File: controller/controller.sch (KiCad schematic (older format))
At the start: 0 parts

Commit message: Add more stuff to controller, start sourcing parts
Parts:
- added U5: ATMEGA328P-AU, TQFP32, symbol ATMEGA328P-AU
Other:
- note added: "TODO: pakeisti kaip reikia Eugenijui\n"

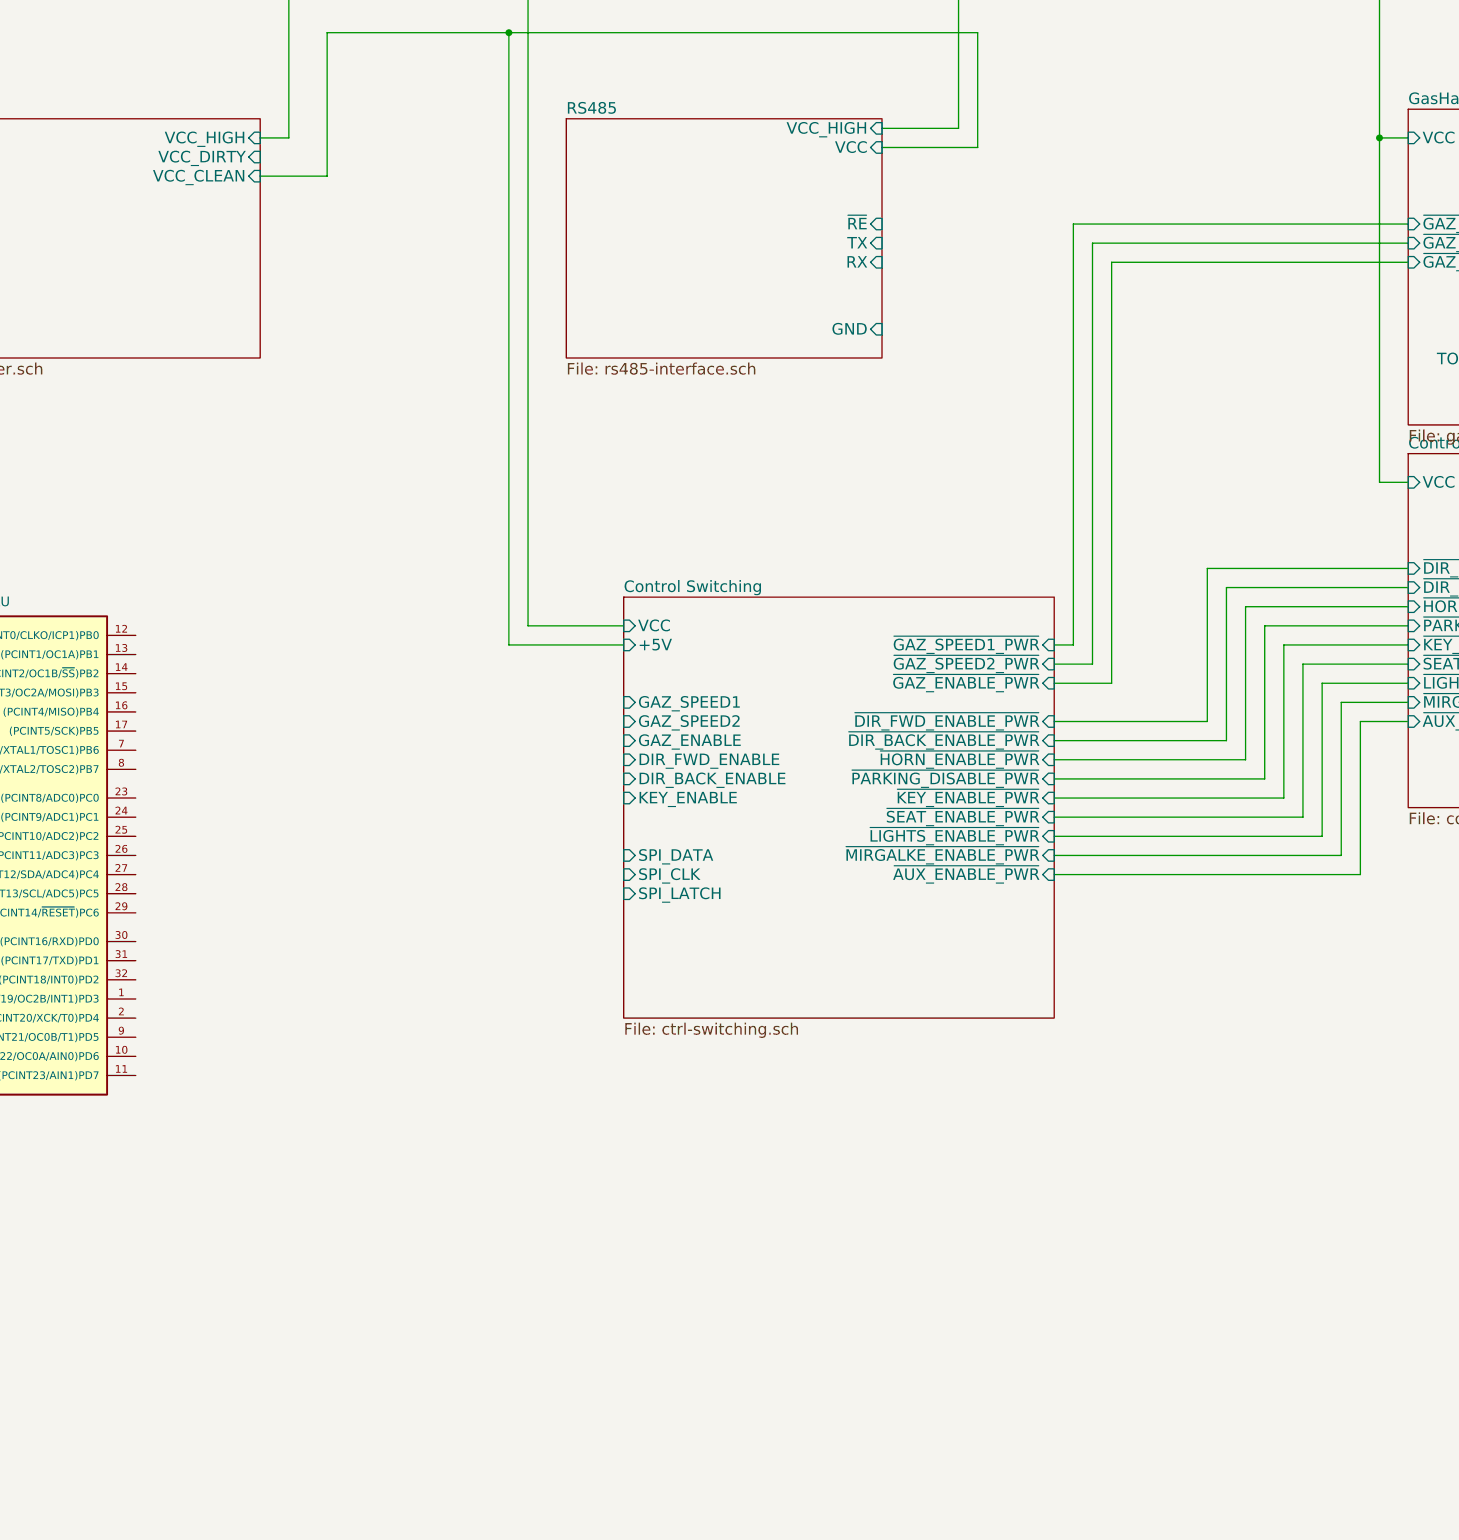
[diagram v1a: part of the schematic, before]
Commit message: Change gas pedal interface so that it supports going up and down from the middle voltage so that it's compatible with Linde forklift gas mechanism
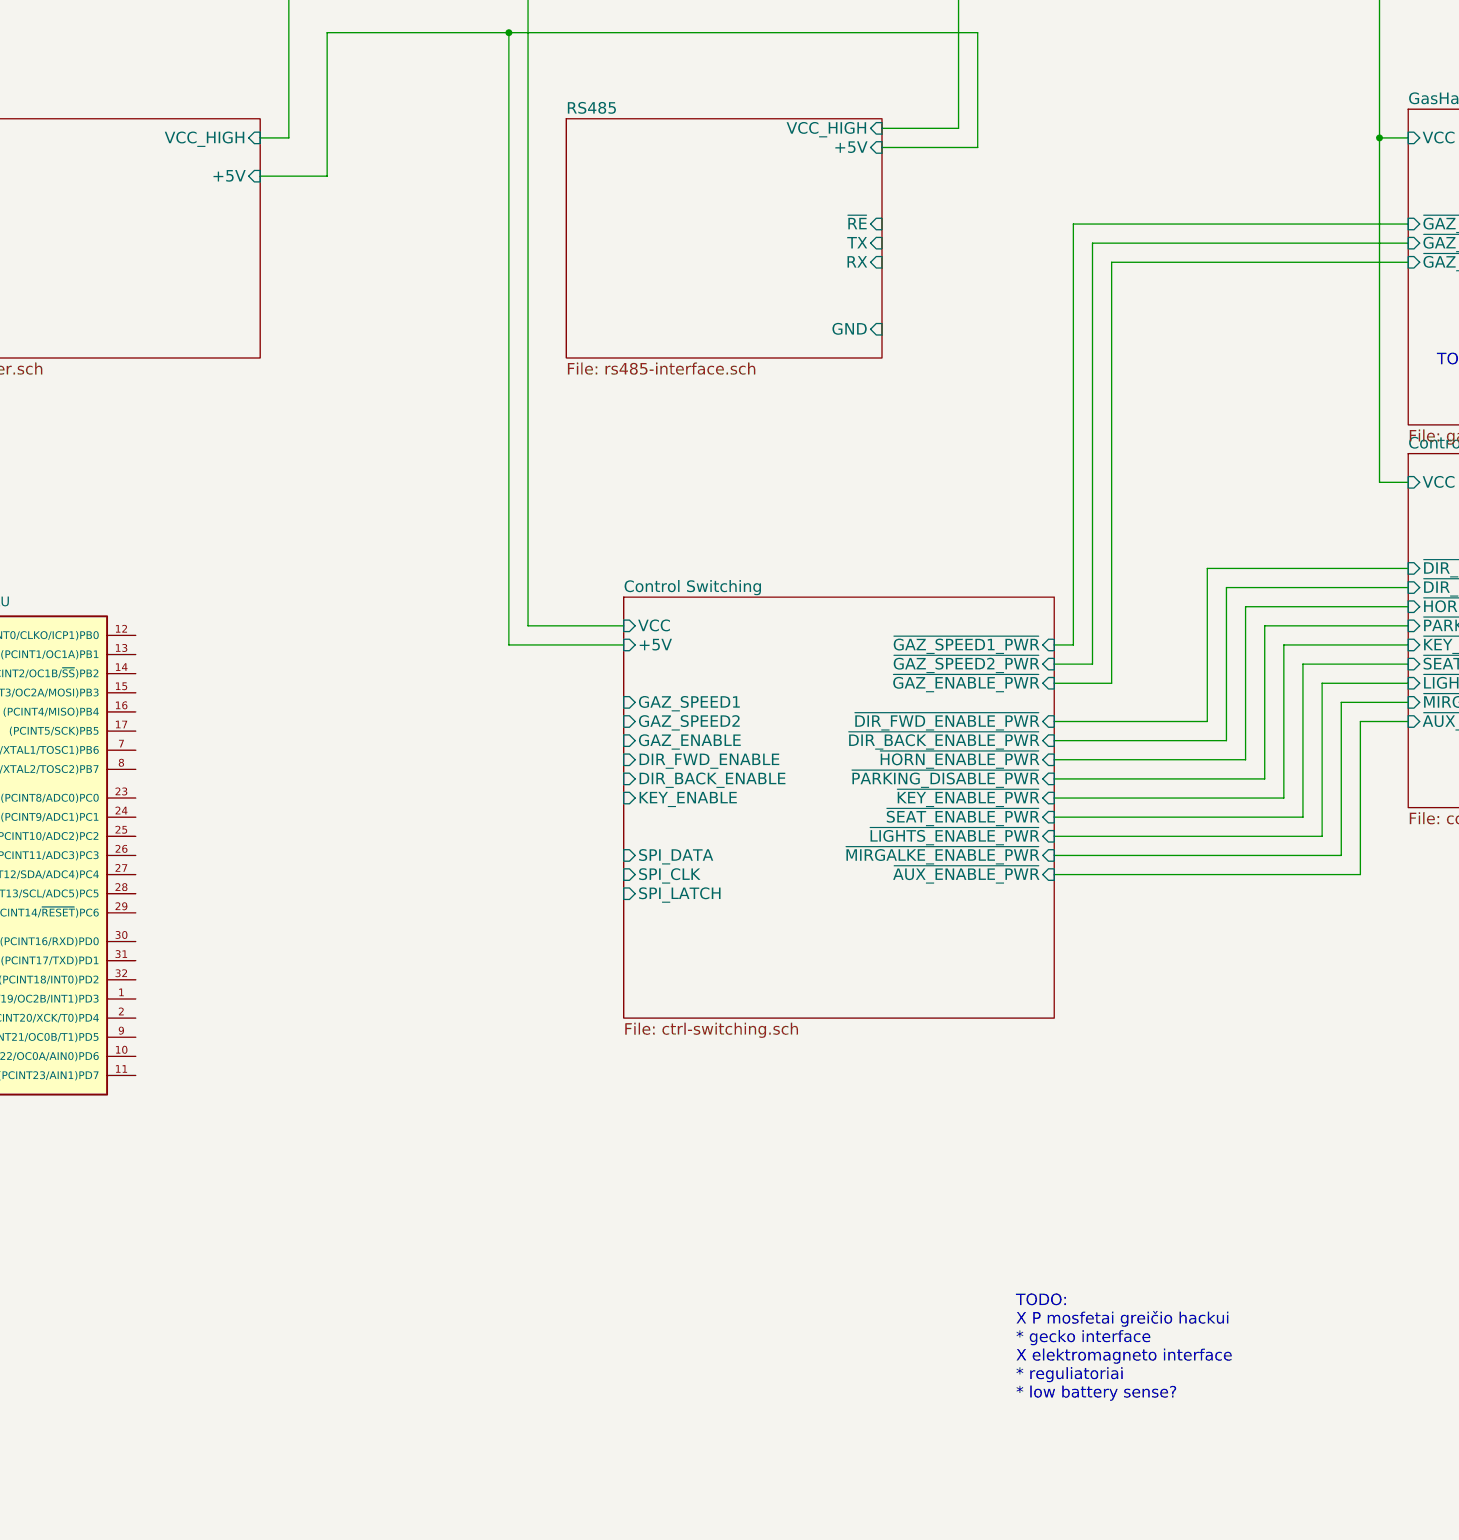
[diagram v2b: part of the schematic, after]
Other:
- note added: "TODO:\nX P mosfetai greičio hackui\n* gecko interface\nX elektromagneto interface\n* reguliatoriai\n* low battery sense?"
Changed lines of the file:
@@
 F3 "TX" I R 10450 4100 60
 F4 "~RE" I R 10450 4000 60
-F5 "VCC" I R 10450 3600 60
+F5 "+5V" I R 10450 3600 60
 F6 "GND" I R 10450 4550 60
 F7 "VCC_HIGH" I R 10450 3500 60
@@
 F0 "Power" 60
 F1 "power.sch" 60
-F2 "VCC_CLEAN" I R 7200 3750 60
-F3 "VCC_DIRTY" I R 7200 3650 60
-F4 "VCC_HIGH" I R 7200 3550 60
-F5 "GND" I L 5450 4600 60
+F2 "+5V" I R 7200 3750 60
+F3 "VCC_HIGH" I R 7200 3550 60
+F4 "GND" I L 5450 4600 60
 $EndSheet
 Wire Wire Line
@@
 	18500 11700 18350 11700
 Connection ~ 18500 4500
+Text Notes 11150 10150 0    60   ~ 0
+TODO:\nX P mosfetai greičio hackui\n* gecko interface\nX elektromagneto interface\n* reguliatoriai\n* low battery sense?
 $EndSCHEMATC

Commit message: More or less final controller board
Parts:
- removed U5: ATMEGA328P-AU, TQFP32, symbol ATMEGA328P-AU
- added MK1, MK2, MK3, MK4: Mounting_Hole, Mounting_Holes:MountingHole_3.2mm_M3, symbol Mounting_Hole
- added SH1: ARDUINO_NANO, w_conn_misc:arduino_nano_header, symbol ARDUINO_NANO
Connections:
- net Control Switching/+5V: now also SH1.5V
- net RS485/RX: now also SH1.0 (RX)
- new net GAZ_ENABLE: SH1.A2
- new net GAZ_SPEED1: SH1.A3
- new net GAZ_SPEED2: SH1.A4
- new net GAZ_SPEED3: SH1.A5
- new net GND: SH1.GND1 (GND/1), SH1.GND2 (2/GND)
- new net HBRIDGE_CURRENT_ANALOG: SH1.A7
- new net KEY_ENABLE: SH1.A1
- new net LINEAR_ACTUATOR_DIRECTION: SH1.8
- new net LINEAR_ACTUATOR_ENABLE: SH1.9 (9_(*))
- new net SPI_CLK: SH1.13 (13_(SCK))
- new net SPI_DATA: SH1.11 (11_(MISO/*))
- new net SPI_LATCH: SH1.10 (10_(SS/*))
- new net STEERING_DIR: SH1.5 (5_(*))
- new net STEERING_ENABLE: SH1.7
- new net STEERING_FAULT: SH1.4
- new net STEERING_STEP: SH1.6 (6_(*))
- new net TAKEOVER: SH1.A0
- new net WHEEL_POS_ANALOG: SH1.A6
- new net ~RE: SH1.2
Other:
- note added: "TODO:\nX P mosfetai greičio hackui\nX gecko interface\nX elektromagneto interface\nX reguliatoriai\n* low battery sense?"
- note removed: "TODO: pakeisti kaip reikia Eugenijui\n"
- note removed: "TODO:\nX P mosfetai greičio hackui\n* gecko interface\nX elektromagneto interface\n* reguliatoriai\n* low battery sense?"
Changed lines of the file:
@@
 LIBS:valves
 LIBS:mic-parts
+LIBS:shield_arduino
 LIBS:controller-cache
 EELAYER 26 0
@@
 F9 "PEDAL_SWITCH_NO" I R 15200 3700 60
 F10 "~GAZ_SPEED2_PWR" I L 13200 4100 60
-F11 "~GAZ_ENABLE_PWR" I L 13200 4200 60
+F11 "~GAZ_ENABLE_PWR" I L 13200 4300 60
+F12 "~GAZ_SPEED3_PWR" I L 13200 4200 60
 $EndSheet
 $Sheet
@@
 F0 "Stepper Interface" 60
 F1 "stepper-interface.sch" 60
+F2 "+5V" I R 18350 9650 60
+F3 "STEERING_ENABLE" I L 16600 9650 60
+F4 "STEERING_STEP" I L 16600 9750 60
+F5 "STEERING_DIR" I L 16600 9850 60
+F6 "STEERING_FAULT" I L 16600 9950 60
 $EndSheet
 $Sheet
@@
 F9 "~MIRGALKE_ENABLE_PWR" I R 11350 7300 60
 F10 "~AUX_ENABLE_PWR" I R 11350 7400 60
-F11 "~GAZ_ENABLE_PWR" I R 11350 6400 60
+F11 "~GAZ_ENABLE_PWR" I R 11350 6500 60
 F12 "~GAZ_SPEED2_PWR" I R 11350 6300 60
 F13 "~GAZ_SPEED1_PWR" I R 11350 6200 60
-F14 "DIR_FWD_ENABLE" I L 9100 6800 60
-F15 "DIR_BACK_ENABLE" I L 9100 6900 60
-F16 "VCC" I L 9100 6100 60
-F17 "GAZ_ENABLE" I L 9100 6700 60
-F18 "GAZ_SPEED2" I L 9100 6600 60
-F19 "GAZ_SPEED1" I L 9100 6500 60
-F20 "KEY_ENABLE" I L 9100 7000 60
-F21 "SPI_DATA" I L 9100 7300 60
-F22 "SPI_CLK" I L 9100 7400 60
-F23 "SPI_LATCH" I L 9100 7500 60
-F24 "+5V" I L 9100 6200 60
-$EndSheet
-Text Notes 13350 4750 0    60   ~ 0
-TODO: pakeisti kaip reikia Eugenijui\n
-$Comp
-L ATMEGA328P-AU U5
-U 1 1 58D08F5A
-P 5550 7250
-F 0 "U5" H 5600 8617 50  0000 C CNN
-F 1 "ATMEGA328P-AU" H 5600 8526 50  0000 C CNN
-F 2 "TQFP32" H -4050 2800 50  0001 C CIN
-F 3 "" H -4050 2800 50  0001 C CNN
-	1    5550 7250
-	1    0    0    -1
-$EndComp
+F14 "VCC" I L 9100 6100 60
+F15 "GAZ_ENABLE" I L 9100 6700 60
+F16 "GAZ_SPEED2" I L 9100 6500 60
+F17 "GAZ_SPEED1" I L 9100 6400 60
+F18 "KEY_ENABLE" I L 9100 6800 60
+F19 "SPI_DATA" I L 9100 7300 60
+F20 "SPI_CLK" I L 9100 7400 60
+F21 "SPI_LATCH" I L 9100 7500 60
+F22 "+5V" I L 9100 6200 60
+F23 "~GAZ_SPEED3_PWR" I R 11350 6400 60
+F24 "GAZ_SPEED3" I L 9100 6600 60
+$EndSheet
 Wire Wire Line
 	9100 6100 8600 6100
@@
 Connection ~ 18500 4500
 Text Notes 11150 10150 0    60   ~ 0
-TODO:\nX P mosfetai greičio hackui\n* gecko interface\nX elektromagneto interface\n* reguliatoriai\n* low battery sense?
+TODO:\nX P mosfetai greičio hackui\nX gecko interface\nX elektromagneto interface\nX reguliatoriai\n* low battery sense?
+Wire Wire Line
+	11350 6500 11750 6500
+Wire Wire Line
+	11750 6500 11750 4300
+Wire Wire Line
+	11750 4300 13200 4300
+$Comp
+L Mounting_Hole MK1
+U 1 1 58C980C4
+P 1000 14950
+F 0 "MK1" H 1100 14996 50  0000 L CNN
+F 1 "Mounting_Hole" H 1100 14905 50  0000 L CNN
+F 2 "Mounting_Holes:MountingHole_3.2mm_M3" H -5850 13300 50  0001 C CNN
+F 3 "" H -5850 13300 50  0001 C CNN
+F 4 "?" H 1000 14950 60  0001 C CNN "PartNo"
+F 5 "?" H 1000 14950 60  0001 C CNN "Manufacturer"
+F 6 "?" H 1000 14950 60  0001 C CNN "Distributor"
+	1    1000 14950
+	1    0    0    -1
+$EndComp
+$Comp
+L Mounting_Hole MK2
+U 1 1 58C980CE
+P 1000 15150
+F 0 "MK2" H 1100 15196 50  0000 L CNN
+F 1 "Mounting_Hole" H 1100 15105 50  0000 L CNN
+F 2 "Mounting_Holes:MountingHole_3.2mm_M3" H -5850 13500 50  0001 C CNN
+F 3 "" H -5850 13500 50  0001 C CNN
+F 4 "?" H 1000 15150 60  0001 C CNN "PartNo"
+F 5 "?" H 1000 15150 60  0001 C CNN "Manufacturer"
+F 6 "?" H 1000 15150 60  0001 C CNN "Distributor"
+	1    1000 15150
+	1    0    0    -1
+$EndComp
+$Comp
+L Mounting_Hole MK3
+U 1 1 58C980D8
+P 1000 15350
+F 0 "MK3" H 1100 15396 50  0000 L CNN
+F 1 "Mounting_Hole" H 1100 15305 50  0000 L CNN
+F 2 "Mounting_Holes:MountingHole_3.2mm_M3" H -5850 13700 50  0001 C CNN
+F 3 "" H -5850 13700 50  0001 C CNN
+F 4 "?" H 1000 15350 60  0001 C CNN "PartNo"
+F 5 "?" H 1000 15350 60  0001 C CNN "Manufacturer"
+F 6 "?" H 1000 15350 60  0001 C CNN "Distributor"
+	1    1000 15350
+	1    0    0    -1
+$EndComp
+$Comp
+L Mounting_Hole MK4
+U 1 1 58C980E2
+P 1000 15550
+F 0 "MK4" H 1100 15596 50  0000 L CNN
+F 1 "Mounting_Hole" H 1100 15505 50  0000 L CNN
+F 2 "Mounting_Holes:MountingHole_3.2mm_M3" H -5850 13900 50  0001 C CNN
+F 3 "" H -5850 13900 50  0001 C CNN
+F 4 "?" H 1000 15550 60  0001 C CNN "PartNo"
+F 5 "?" H 1000 15550 60  0001 C CNN "Manufacturer"
+F 6 "?" H 1000 15550 60  0001 C CNN "Distributor"
+	1    1000 15550
+	1    0    0    -1
+$EndComp
+$Comp
+L ARDUINO_NANO SH1
+U 1 1 58C7F268
+P 7200 9800
+F 0 "SH1" H 7200 10937 60  0000 C CNN
+F 1 "ARDUINO_NANO" H 7200 10831 60  0000 C CNN
+F 2 "w_conn_misc:arduino_nano_header" H 6275 9200 60  0000 C CNN
+F 3 "" H 6275 9200 60  0000 C CNN
+F 4 "?" H 7200 9800 60  0001 C CNN "PartNo"
+F 5 "?" H 7200 9800 60  0001 C CNN "Manufacturer"
+F 6 "?" H 7200 9800 60  0001 C CNN "Distributor"
+	1    7200 9800
+	1    0    0    -1
+$EndComp
+Wire Wire Line
+	10450 4200 10600 4200
+Wire Wire Line
+	10600 4200 10600 5000
+Wire Wire Line
+	10600 5000 6350 5000
+Wire Wire Line
+	6350 5000 6350 9050
+Wire Wire Line
+	6350 9050 6550 9050
+Wire Wire Line
+	10450 4150 10650 4150
+Wire Wire Line
+	10650 4150 10650 5100
+Wire Wire Line
+	10650 5100 6450 5100
+Wire Wire Line
+	6450 5100 6450 8950
+Wire Wire Line
+	6450 8950 6550 8950
+Text HLabel 7850 10350 2    60   Input ~ 0
+HBRIDGE_CURRENT_ANALOG
+Text HLabel 7850 10200 2    60   Input ~ 0
+WHEEL_POS_ANALOG
+Text HLabel 6550 10550 0    60   Input ~ 0
+SPI_DATA
+Text HLabel 7850 10700 2    60   Input ~ 0
+SPI_CLK
+Text HLabel 7850 9600 2    60   Input ~ 0
+KEY_ENABLE
+Text HLabel 7850 9700 2    60   Input ~ 0
+GAZ_ENABLE
+Text HLabel 7850 9950 2    60   Input ~ 0
+GAZ_SPEED2
+Text HLabel 7850 9850 2    60   Input ~ 0
+GAZ_SPEED1
+Text HLabel 7850 10100 2    60   Input ~ 0
+GAZ_SPEED3
+Text HLabel 6550 10450 0    60   Input ~ 0
+SPI_LATCH
+Text HLabel 7850 9450 2    60   Input ~ 0
+TAKEOVER
+Text HLabel 6550 10050 0    60   Input ~ 0
+STEERING_ENABLE
+Text HLabel 6550 9950 0    60   Input ~ 0
+STEERING_STEP
+Text HLabel 6550 9800 0    60   Input ~ 0
+STEERING_DIR
+Text HLabel 6550 9700 0    60   Input ~ 0
+STEERING_FAULT
+Text HLabel 6550 9450 0    60   Input ~ 0
+~RE
+Text HLabel 6550 10300 0    60   Input ~ 0
+LINEAR_ACTUATOR_ENABLE
+Text HLabel 6550 10200 0    60   Input ~ 0
+LINEAR_ACTUATOR_DIRECTION
+$Comp
+L GND #PWR01
+U 1 1 58CADA03
+P 8300 9050
+F 0 "#PWR01" H 8300 8800 50  0001 C CNN
+F 1 "GND" H 8305 8877 50  0000 C CNN
+F 2 "" H 8300 9050 50  0001 C CNN
+F 3 "" H 8300 9050 50  0001 C CNN
+	1    8300 9050
+	1    0    0    -1
+$EndComp
+Wire Wire Line
+	8300 9050 7850 9050
+Wire Wire Line
+	7850 9300 8100 9300
+Wire Wire Line
+	8100 9300 8100 3000
+Connection ~ 8100 3000
+$Comp
+L GND #PWR02
+U 1 1 58CAF659
+P 6100 9300
+F 0 "#PWR02" H 6100 9050 50  0001 C CNN
+F 1 "GND" H 6105 9127 50  0000 C CNN
+F 2 "" H 6100 9300 50  0001 C CNN
+F 3 "" H 6100 9300 50  0001 C CNN
+	1    6100 9300
+	1    0    0    -1
+$EndComp
+Wire Wire Line
+	6100 9300 6550 9300
 $EndSCHEMATC

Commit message: Finish the routing, add some significant fixes: *correct to-252 pin numbering * longer pads for relays * fix footprint of the optocouplers
Also finish the routing
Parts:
- SH1: footprint w_conn_misc:arduino_nano_header -> SHIELD_ARDUINO:ARDUINO_NANO_2_CONTOUR_ELL
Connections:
- net GAZ_ENABLE is gone; now on net Control Switching/GAZ_ENABLE: SH1.A2
- net KEY_ENABLE is gone; now on net Control Switching/KEY_ENABLE: SH1.A1
- net TAKEOVER is gone; now on net Takeover/TAKEOVER: SH1.A0
- net HBRIDGE_CURRENT_ANALOG: now also SH1.A6; no longer SH1.A7
- net RS485/TX: now also SH1.1 (TX)
- net WHEEL_POS_ANALOG: now also SH1.A7; no longer SH1.A6
- net Break H bridge/MAGNET_ENGAGE: now reaches SH1.3 (3_(*))
